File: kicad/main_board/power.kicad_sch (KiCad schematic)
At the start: 41 parts, among them Q1 DMN63D8LW, Q2 DMP3018SFV, SW1 SW_Push, U4 TPS560430, U5 TPS560430

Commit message: add input
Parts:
- renumbered C20 to C10, C21 to C11, C22 to C12, C23 to C13, C24 to C14, C25 to C15, C17 to C7, C18 to C8, C19 to C9, D1 to D2, D2 to D3, D3 to D4, D4 to D5, D5 to D6, D6 to D7, JP6 to JP1, Q1 to Q3, Q2 to Q4, R14 to R18, R15 to R19, R16 to R20, R17 to R21, R18 to R22, R19 to R23, R20 to R24, R21 to R25, R22 to R26, TP14 to TP10, TP15 to TP11, TP16 to TP12, TP17 to TP13, TP18 to TP14, TP19 to TP15, TP11 to TP7, TP12 to TP8, TP13 to TP9

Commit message: add audio
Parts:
- renumbered TP11 to TP10, TP12 to TP11, TP13 to TP12, TP14 to TP13, TP15 to TP14, TP7 to TP6, TP8 to TP7, TP9 to TP8, TP10 to TP9
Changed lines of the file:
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@@
 		(dnp no)
 		(fields_autoplaced yes)
-		(property "Reference" "TP14"
+		(property "Reference" "TP13"
 			(at 266.7 43.18 0)
 			(effects
@@
 			(project "main_board"
 				(path "/8e1f1504-76c2-49e6-9261-3c1190503f8c/afe2ed97-1c60-4e5a-9a63-45f783bd4ddb"
-					(reference "TP14")
+					(reference "TP13")
 					(unit 1)
 				)
@@
 		(dnp no)
 		(fields_autoplaced yes)
-		(property "Reference" "TP9"
+		(property "Reference" "TP8"
 			(at 185.42 153.67 0)
 			(effects
@@
 			(project "main_board"
 				(path "/8e1f1504-76c2-49e6-9261-3c1190503f8c/afe2ed97-1c60-4e5a-9a63-45f783bd4ddb"
-					(reference "TP9")
+					(reference "TP8")
 					(unit 1)
 				)
@@
 		(dnp no)
 		(fields_autoplaced yes)
-		(property "Reference" "TP7"
+		(property "Reference" "TP6"
 			(at 137.16 48.26 90)
 			(effects
@@
 			(project "main_board"
 				(path "/8e1f1504-76c2-49e6-9261-3c1190503f8c/afe2ed97-1c60-4e5a-9a63-45f783bd4ddb"
-					(reference "TP7")
+					(reference "TP6")
 					(unit 1)
 				)
@@
 		(dnp no)
 		(fields_autoplaced yes)
-		(property "Reference" "TP12"
+		(property "Reference" "TP11"
 			(at 196.85 43.18 0)
 			(effects
@@
 			(project "main_board"
 				(path "/8e1f1504-76c2-49e6-9261-3c1190503f8c/afe2ed97-1c60-4e5a-9a63-45f783bd4ddb"
-					(reference "TP12")
+					(reference "TP11")
 					(unit 1)
 				)
@@
 		(dnp no)
 		(fields_autoplaced yes)
-		(property "Reference" "TP8"
+		(property "Reference" "TP7"
 			(at 184.15 80.01 0)
 			(effects
@@
 			(project "main_board"
 				(path "/8e1f1504-76c2-49e6-9261-3c1190503f8c/afe2ed97-1c60-4e5a-9a63-45f783bd4ddb"
-					(reference "TP8")
+					(reference "TP7")
 					(unit 1)
 				)
@@
 		(dnp no)
 		(fields_autoplaced yes)
-		(property "Reference" "TP13"
+		(property "Reference" "TP12"
 			(at 198.12 121.92 0)
 			(effects
@@
 			(project "main_board"
 				(path "/8e1f1504-76c2-49e6-9261-3c1190503f8c/afe2ed97-1c60-4e5a-9a63-45f783bd4ddb"
-					(reference "TP13")
+					(reference "TP12")
 					(unit 1)
 				)
@@
 		(dnp no)
 		(fields_autoplaced yes)
-		(property "Reference" "TP10"
+		(property "Reference" "TP9"
 			(at 193.04 80.01 0)
 			(effects
@@
 			(project "main_board"
 				(path "/8e1f1504-76c2-49e6-9261-3c1190503f8c/afe2ed97-1c60-4e5a-9a63-45f783bd4ddb"
-					(reference "TP10")
+					(reference "TP9")
 					(unit 1)
 				)
@@
 		(dnp no)
 		(fields_autoplaced yes)
-		(property "Reference" "TP11"
+		(property "Reference" "TP10"
 			(at 193.04 153.67 0)
 			(effects
@@
 			(project "main_board"
 				(path "/8e1f1504-76c2-49e6-9261-3c1190503f8c/afe2ed97-1c60-4e5a-9a63-45f783bd4ddb"
-					(reference "TP11")
+					(reference "TP10")
 					(unit 1)
 				)
@@
 		(dnp no)
 		(fields_autoplaced yes)
-		(property "Reference" "TP15"
+		(property "Reference" "TP14"
 			(at 267.97 121.92 0)
 			(effects
@@
 			(project "main_board"
 				(path "/8e1f1504-76c2-49e6-9261-3c1190503f8c/afe2ed97-1c60-4e5a-9a63-45f783bd4ddb"
-					(reference "TP15")
+					(reference "TP14")
 					(unit 1)
 				)

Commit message: add charger
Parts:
- renumbered C7 to C42, C8 to C43, C9 to C44, C10 to C45, C11 to C46, C12 to C47, C13 to C48, C14 to C49, C15 to C50, D2 to D3, D3 to D4, D4 to D5, D5 to D6, D6 to D7, D7 to D8, JP1 to JP2, L1 to L2, L2 to L3, Q3 to Q8, Q4 to Q9, R18 to R37, R19 to R38, R20 to R39, R21 to R40, R22 to R41, R23 to R42, R24 to R43, R25 to R44, R26 to R45, TP6 to TP13, TP7 to TP14, TP8 to TP15, TP9 to TP16, TP10 to TP17, TP11 to TP18, TP12 to TP19, TP13 to TP20, TP14 to TP21, U4 to U5, U5 to U6

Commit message: add I2S link
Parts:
- renumbered TP13 to TP14, TP14 to TP15, TP15 to TP16, TP16 to TP17, TP17 to TP18, TP18 to TP19, TP19 to TP20, TP20 to TP21, TP21 to TP22
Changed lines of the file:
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@@
 	(title_block
 		(title "SW32 - Main Board")
-		(date "2024-05-22")
+		(date "2024-05-23")
 		(rev "1")
 		(company "saawsm")
@@
 		(dnp no)
 		(fields_autoplaced yes)
-		(property "Reference" "TP20"
+		(property "Reference" "TP21"
 			(at 266.7 43.18 0)
 			(effects
@@
 			(project "main_board"
 				(path "/8e1f1504-76c2-49e6-9261-3c1190503f8c/afe2ed97-1c60-4e5a-9a63-45f783bd4ddb"
-					(reference "TP20")
+					(reference "TP21")
 					(unit 1)
 				)
@@
 		(dnp no)
 		(fields_autoplaced yes)
-		(property "Reference" "TP15"
+		(property "Reference" "TP16"
 			(at 185.42 153.67 0)
 			(effects
@@
 			(project "main_board"
 				(path "/8e1f1504-76c2-49e6-9261-3c1190503f8c/afe2ed97-1c60-4e5a-9a63-45f783bd4ddb"
-					(reference "TP15")
+					(reference "TP16")
 					(unit 1)
 				)
@@
 		(dnp no)
 		(fields_autoplaced yes)
-		(property "Reference" "TP13"
+		(property "Reference" "TP14"
 			(at 137.16 48.26 90)
 			(effects
@@
 			(project "main_board"
 				(path "/8e1f1504-76c2-49e6-9261-3c1190503f8c/afe2ed97-1c60-4e5a-9a63-45f783bd4ddb"
-					(reference "TP13")
+					(reference "TP14")
 					(unit 1)
 				)
@@
 		(dnp no)
 		(fields_autoplaced yes)
-		(property "Reference" "TP18"
+		(property "Reference" "TP19"
 			(at 196.85 43.18 0)
 			(effects
@@
 			(project "main_board"
 				(path "/8e1f1504-76c2-49e6-9261-3c1190503f8c/afe2ed97-1c60-4e5a-9a63-45f783bd4ddb"
-					(reference "TP18")
+					(reference "TP19")
 					(unit 1)
 				)
@@
 		(dnp no)
 		(fields_autoplaced yes)
-		(property "Reference" "TP14"
+		(property "Reference" "TP15"
 			(at 184.15 80.01 0)
 			(effects
@@
 			(project "main_board"
 				(path "/8e1f1504-76c2-49e6-9261-3c1190503f8c/afe2ed97-1c60-4e5a-9a63-45f783bd4ddb"
-					(reference "TP14")
+					(reference "TP15")
 					(unit 1)
 				)
@@
 		(dnp no)
 		(fields_autoplaced yes)
-		(property "Reference" "TP19"
+		(property "Reference" "TP20"
 			(at 198.12 121.92 0)
 			(effects
@@
 			(project "main_board"
 				(path "/8e1f1504-76c2-49e6-9261-3c1190503f8c/afe2ed97-1c60-4e5a-9a63-45f783bd4ddb"
-					(reference "TP19")
+					(reference "TP20")
 					(unit 1)
 				)
@@
 		(dnp no)
 		(fields_autoplaced yes)
-		(property "Reference" "TP16"
+		(property "Reference" "TP17"
 			(at 193.04 80.01 0)
 			(effects
@@
 			(project "main_board"
 				(path "/8e1f1504-76c2-49e6-9261-3c1190503f8c/afe2ed97-1c60-4e5a-9a63-45f783bd4ddb"
-					(reference "TP16")
+					(reference "TP17")
 					(unit 1)
 				)
@@
 		(dnp no)
 		(fields_autoplaced yes)
-		(property "Reference" "TP17"
+		(property "Reference" "TP18"
 			(at 193.04 153.67 0)
 			(effects
@@
 			(project "main_board"
 				(path "/8e1f1504-76c2-49e6-9261-3c1190503f8c/afe2ed97-1c60-4e5a-9a63-45f783bd4ddb"
-					(reference "TP17")
+					(reference "TP18")
 					(unit 1)
 				)
@@
 		(dnp no)
 		(fields_autoplaced yes)
-		(property "Reference" "TP21"
+		(property "Reference" "TP22"
 			(at 267.97 121.92 0)
 			(effects
@@
 			(project "main_board"
 				(path "/8e1f1504-76c2-49e6-9261-3c1190503f8c/afe2ed97-1c60-4e5a-9a63-45f783bd4ddb"
-					(reference "TP21")
+					(reference "TP22")
 					(unit 1)
 				)

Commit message: remove BAT_INT
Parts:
- renumbered D3 to D2, D4 to D3, D5 to D4, D6 to D5, D7 to D6, D8 to D7, R37 to R36, R38 to R37, R39 to R38, R40 to R39, R41 to R40, R42 to R41, R43 to R42, R44 to R43, R45 to R44, TP14 to TP13, TP15 to TP14, TP16 to TP15, TP17 to TP16, TP18 to TP17, TP19 to TP18, TP20 to TP19, TP21 to TP20, TP22 to TP21

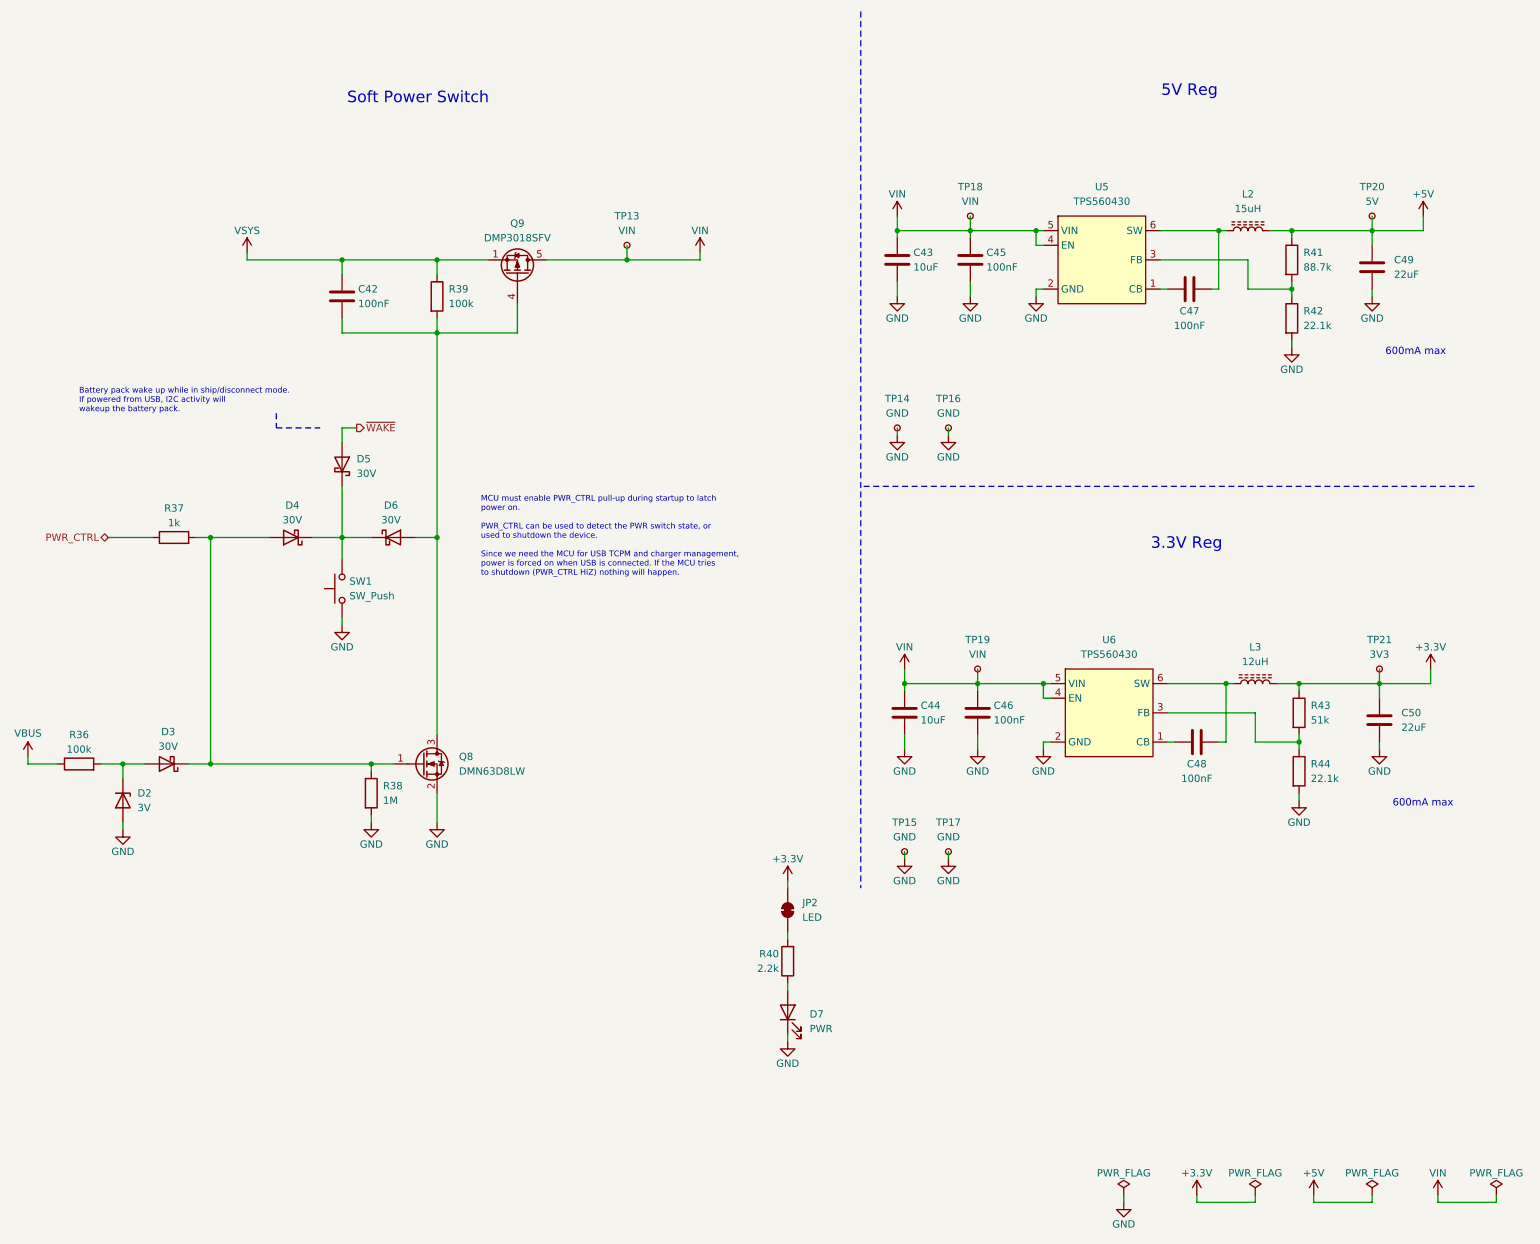
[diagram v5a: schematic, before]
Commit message: update BOM prioritizing basic parts
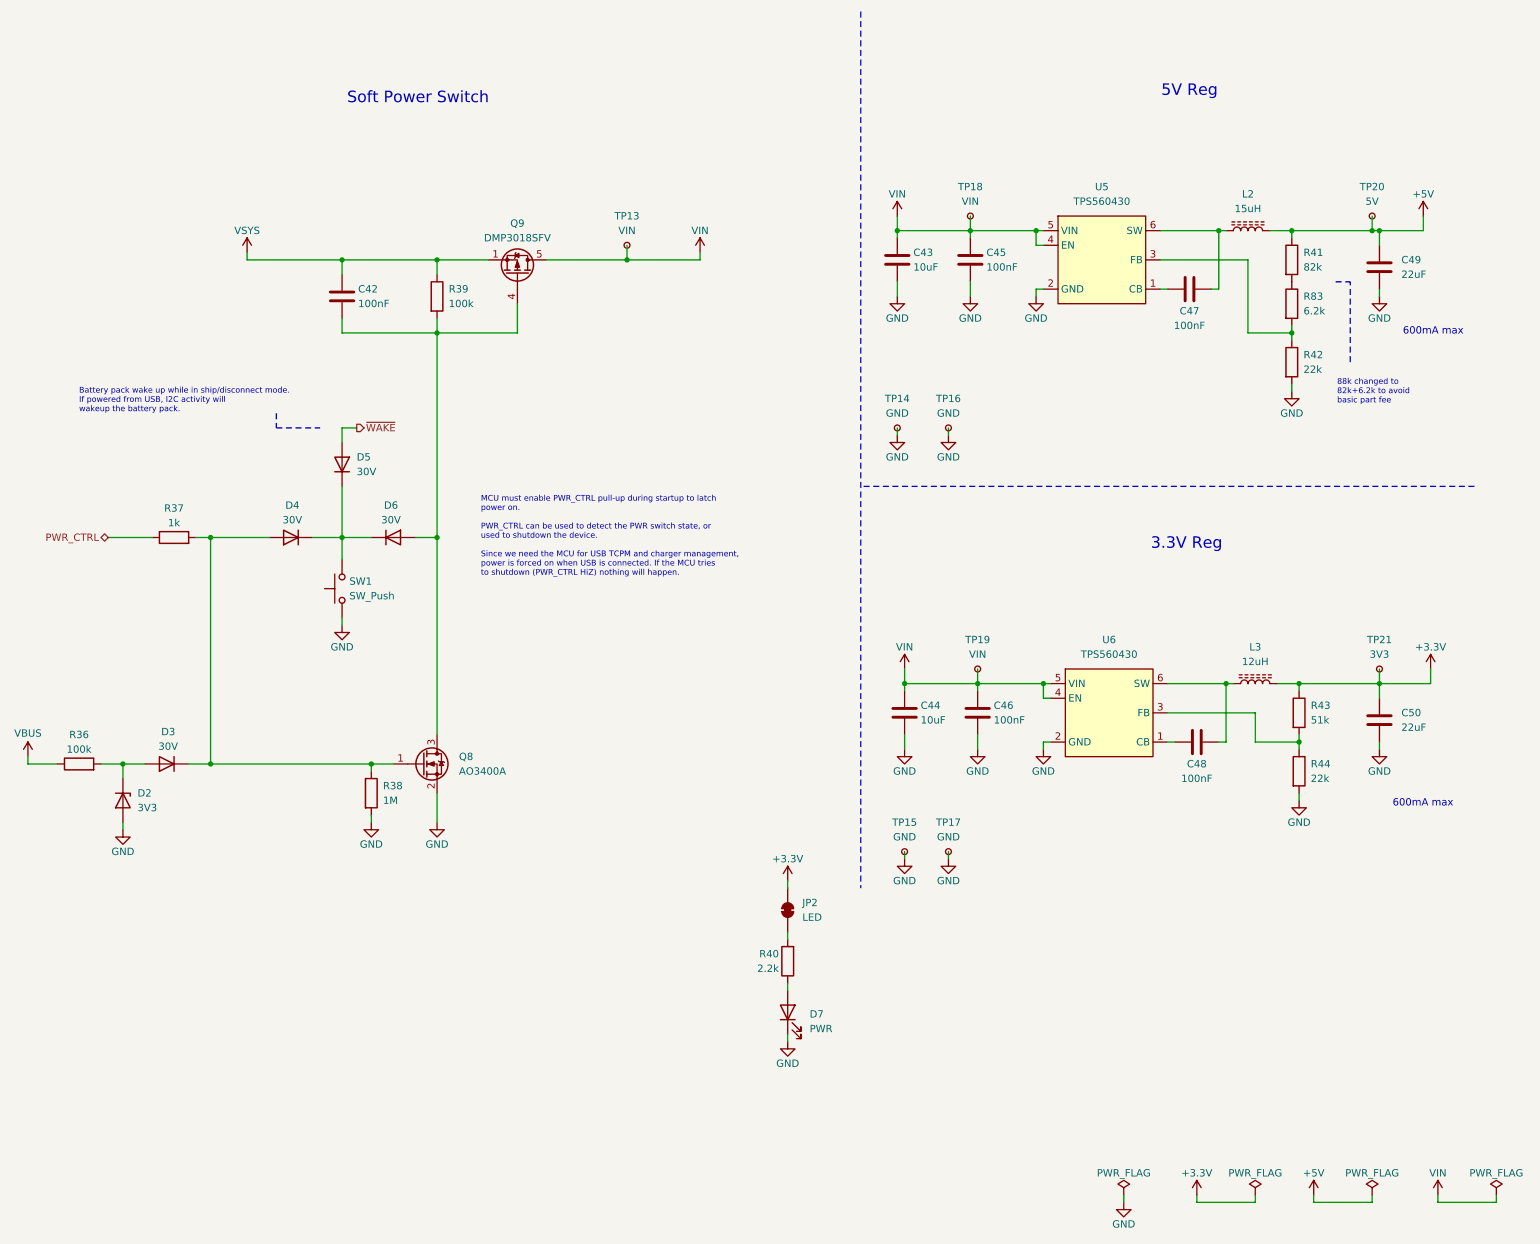
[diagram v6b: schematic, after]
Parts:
- added R83: 6.2k, Resistor_SMD:R_0603_1608Metric, symbol Device:R
- C42, C45, C46, C47, C48: JLC (none) -> C14663; LCSC C1591 -> (none); MOUSER 187-CL10B104KB8NNNC -> (none); MPN CL10B104KB8NNNC -> (none)
- C43, C44: JLC (none) -> C440198; LCSC C2932476 -> (none); MOUSER 187-CL21A106KBYQNNE -> (none); MPN CL21A106KBYQNNE -> (none)
- C49, C50: JLC (none) -> C45783; LCSC C602037 -> (none); MOUSER 187-CL21A226MAYNNNE -> (none); MPN CL21A226MAYNNNE -> (none)
- D2: value 3V -> 3V3; footprint Diode_SMD:D_SOD-523 -> Diode_SMD:D_SOD-323; JLC (none) -> C391441; LCSC C5248671 -> (none); MOUSER 621-BZT52C3V0T-7 -> (none); MPN BZT52C3V0T-7 -> (none)
- D3, D4, D5, D6: footprint Diode_SMD:D_SOD-523 -> Diode_SMD:D_SOD-323; symbol Device:D_Schottky -> Device:D; JLC (none) -> C2128; LCSC C232575 -> (none); MOUSER 863-RB520S30T5G -> (none); MPN RB520S30T5G -> (none)
- D7: JLC (none) -> C2286
- L2: JLC (none) -> C1330797; LCSC C1330797 -> (none); MOUSER 652-SRN6045TA-150M -> (none); MPN SRN6045TA-150M -> (none)
- L3: JLC (none) -> C2049956; LCSC C2049956 -> (none); MOUSER 652-SRN6045TA-120M -> (none); MPN SRN6045TA-120M -> (none); MPN_ALT SRN6045TA-100M -> (none)
- Q8: value DMN63D8LW -> AO3400A; footprint Package_TO_SOT_SMD:SOT-323_SC-70 -> Package_TO_SOT_SMD:SOT-23; JLC (none) -> C20917; LCSC C151057 -> (none); MOUSER 621-DMN63D8LW-7 -> (none); MPN DMN63D8LW-7 -> (none)
- Q9: JLC (none) -> C461075; LCSC C461075 -> (none); MOUSER 621-DMP3018SFV-7 -> (none); MPN DMP3018SFV-7 -> (none)
- R36, R39: JLC (none) -> C25803; LCSC C25803 -> (none); MOUSER 603-RC0603FR-07100KL -> (none); MPN RC0603FR-07100KL -> (none)
- R37: JLC (none) -> C21190; LCSC C21190 -> (none); MOUSER 603-RC0603FR-071KL -> (none); MPN RC0603FR-071KL -> (none)
- R38: JLC (none) -> C22935; LCSC C22935 -> (none); MOUSER 603-RC0603FR-071ML -> (none); MPN RC0603FR-071ML -> (none)
- R40: JLC (none) -> C4190; LCSC C4190 -> (none); MOUSER 603-RC0603FR-072K2L -> (none); MPN RC0603FR-072K2L -> (none)
- R41: value 88.7k -> 82k; JLC (none) -> C23254; LCSC C23258 -> (none); MOUSER 603-RC0603FR-0788K7L -> (none); MPN RC0603FR-0788K7L -> (none)
- R42, R44: value 22.1k -> 22k; JLC (none) -> C31850; LCSC C25961 -> (none); MOUSER 603-RC0603FR-0722K1L -> (none); MPN RC0603FR-0722K1L -> (none)
- R43: JLC (none) -> C23196; LCSC C23196 -> (none); MOUSER 603-RC0603FR-0751KL -> (none); MPN RC0603FR-0751KL -> (none)
- SW1: footprint Button_Switch_THT:SW_Tactile_SPST_Angled_PTS645Vx58-2LFS -> Button_Switch_THT:SW_Tactile_SPST_Angled_PTS645Vx31-2LFS; LCSC C221887 -> C2804591; MOUSER 611-PTS645VH392 -> (none); MPN PTS645VH392LFS -> (none)
- U5, U6: JLC (none) -> C524782; LCSC C524782 -> (none); MOUSER 595-TPS560430XDBVR -> (none); MPN TPS560430XDBVR -> (none)
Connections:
- net at R42.1, U5.3 (FB): now also R83.2; no longer R41.2
- new net: R41.2, R83.1
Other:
- note added: "88k changed to 82k+6.2k to avoid basic part fee"
- moved on the sheet: C49, R42

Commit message: add generation script
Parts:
- C42, C45, C46, C47, C48: JLC C14663 -> (none); LCSC (none) -> C14663; Service (none) -> PCBA
- C43, C44: JLC C440198 -> (none); LCSC (none) -> C440198; Service (none) -> PCBA
- C49, C50: JLC C45783 -> (none); LCSC (none) -> C45783; Service (none) -> PCBA
- D2: JLC C391441 -> (none); LCSC (none) -> C391441; Service (none) -> PCBA
- D3, D4, D5, D6: JLC C2128 -> (none); LCSC (none) -> C2128; Service (none) -> PCBA
- D7: JLC C2286 -> (none); LCSC (none) -> C2286; Service (none) -> PCBA
- JP2, TP13, TP14, TP15, TP16, TP17, TP18, TP19, TP20, TP21: Service (none) -> PCBA;HandAssembly
- L2: JLC C1330797 -> (none); LCSC (none) -> C1330797; Service (none) -> PCBA
- L3: JLC C2049956 -> (none); LCSC (none) -> C2049956; Service (none) -> PCBA
- Q8: JLC C20917 -> (none); LCSC (none) -> C20917; Service (none) -> PCBA
- Q9: JLC C461075 -> (none); LCSC (none) -> C461075; Service (none) -> PCBA
- R36, R39: JLC C25803 -> (none); LCSC (none) -> C25803; Service (none) -> PCBA
- R37: JLC C21190 -> (none); LCSC (none) -> C21190; Service (none) -> PCBA
- R38: JLC C22935 -> (none); LCSC (none) -> C22935; Service (none) -> PCBA
- R40: JLC C4190 -> (none); LCSC (none) -> C4190; Service (none) -> PCBA
- R41: JLC C23254 -> (none); LCSC (none) -> C23254; Service (none) -> PCBA
- R42, R44: JLC C31850 -> (none); LCSC (none) -> C31850; Service (none) -> PCBA
- R43: JLC C23196 -> (none); LCSC (none) -> C23196; Service (none) -> PCBA
- R83: JLC C4260 -> (none); LCSC (none) -> C4260; Service (none) -> PCBA
- SW1: Service (none) -> HandAssembly
- U5, U6: JLC C524782 -> (none); LCSC (none) -> C524782; Service (none) -> PCBA

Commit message: use same inductor value for both supply rails
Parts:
- L2: value 15uH -> 12uH; footprint Inductor_SMD:L_Bourns_SRN6045TA -> (none); LCSC C1330797 -> C168035
- L3: footprint Inductor_SMD:L_Bourns_SRN6045TA -> (none); LCSC C2049956 -> C168035
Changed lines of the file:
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@@
 			)
 		)
-		(property "Footprint" "Inductor_SMD:L_Bourns_SRN6045TA"
+		(property "Footprint" ""
 			(at 246.38 129.54 0)
 			(effects
@@
 			)
 		)
-		(property "Datasheet" "https://www.bourns.com/docs/Product-Datasheets/SRN6045TA.pdf"
+		(property "Datasheet" "https://www.lcsc.com/datasheet/lcsc_datasheet_2304140030_cjiang--Changjiang-Microelectronics-Tech-FNR6028S120MT_C168035.pdf"
 			(at 246.38 129.54 0)
 			(effects
@@
 			)
 		)
-		(property "LCSC" "C2049956"
+		(property "LCSC" "C168035"
 			(at 246.38 129.54 0)
 			(effects
@@
 			)
 		)
-		(property "Value" "15uH"
+		(property "Value" "12uH"
 			(at 245.11 46.99 90)
 			(effects
@@
 			)
 		)
-		(property "Footprint" "Inductor_SMD:L_Bourns_SRN6045TA"
+		(property "Footprint" ""
 			(at 245.11 50.8 0)
 			(effects
@@
 			)
 		)
-		(property "Datasheet" "https://www.bourns.com/docs/Product-Datasheets/SRN6045TA.pdf"
+		(property "Datasheet" "https://www.lcsc.com/datasheet/lcsc_datasheet_2304140030_cjiang--Changjiang-Microelectronics-Tech-FNR6028S120MT_C168035.pdf"
 			(at 245.11 50.8 0)
 			(effects
@@
 			)
 		)
-		(property "Description" "Semi-shielded Power Inductor with ferrite core"
+		(property "Description" "Semi-shielded Power Inductor"
 			(at 245.11 50.8 0)
 			(effects
@@
 			)
 		)
-		(property "LCSC" "C1330797"
+		(property "LCSC" "C168035"
 			(at 245.11 50.8 0)
 			(effects
